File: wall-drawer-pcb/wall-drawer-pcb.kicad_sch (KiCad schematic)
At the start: 13 parts, among them J1 Conn_01x04_Pin, J2 Conn_01x04_Pin, J3 Conn_01x02_Pin, J4 Conn_01x02_Pin, J5 Conn_PWRJack_2x5.5mm_CUIDevic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, M1 Module_XIAO-ESP32C3, U1 Regulator_Linear_5.0V_1A_OnSe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

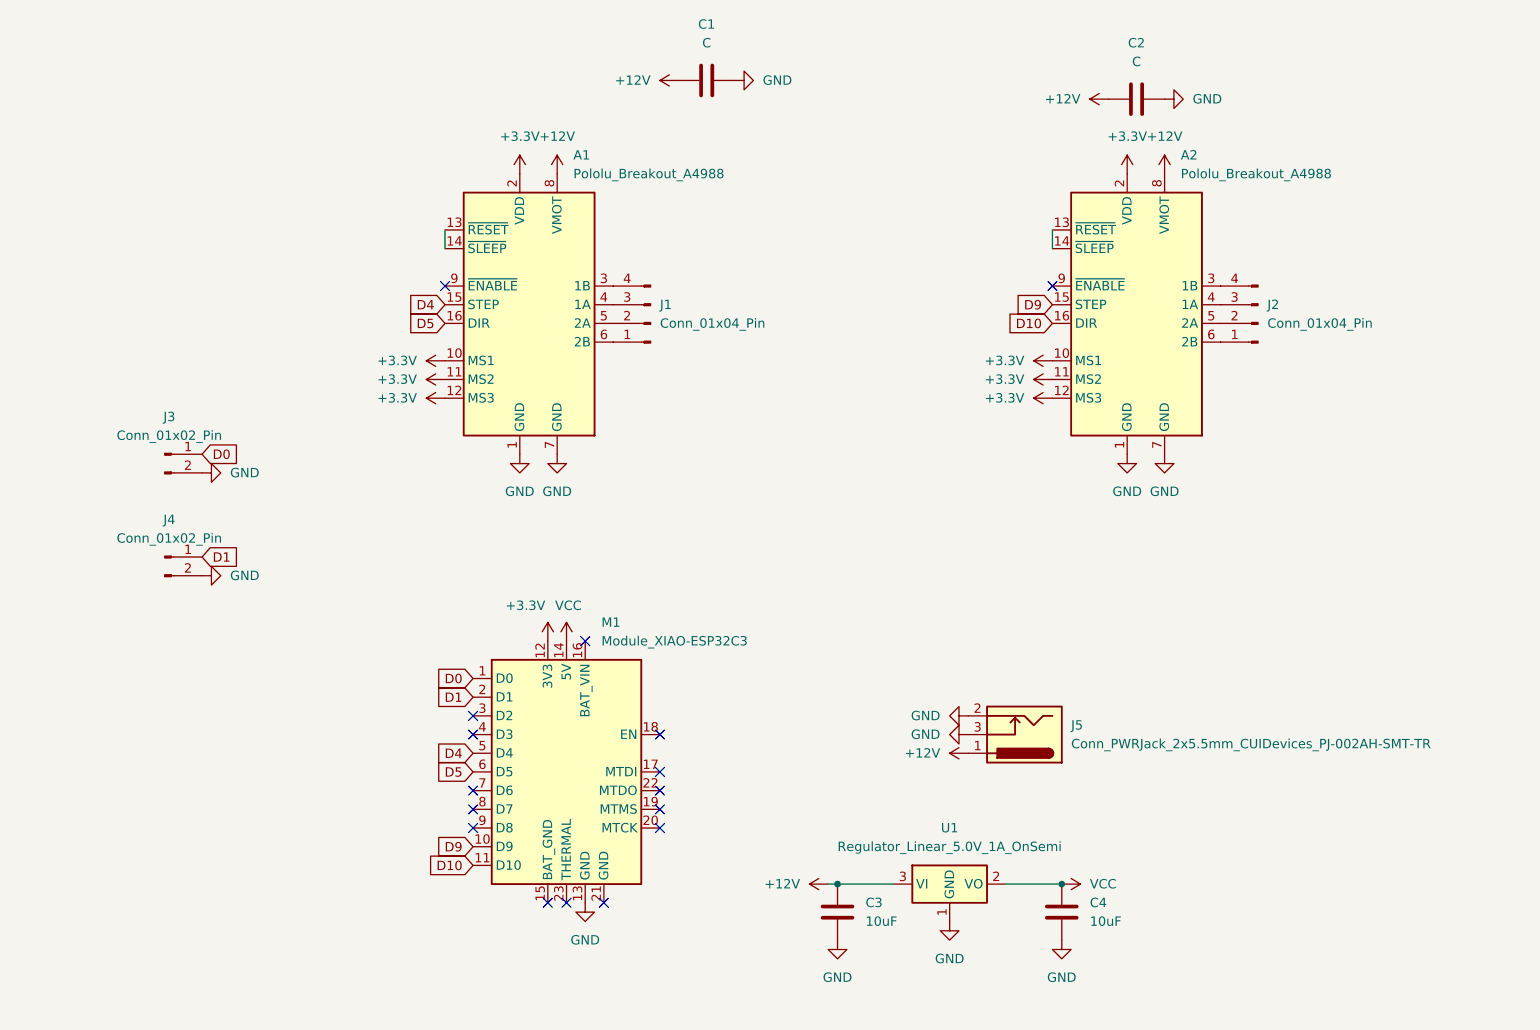
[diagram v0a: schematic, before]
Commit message: wall drawer pcb to use tmc2209s
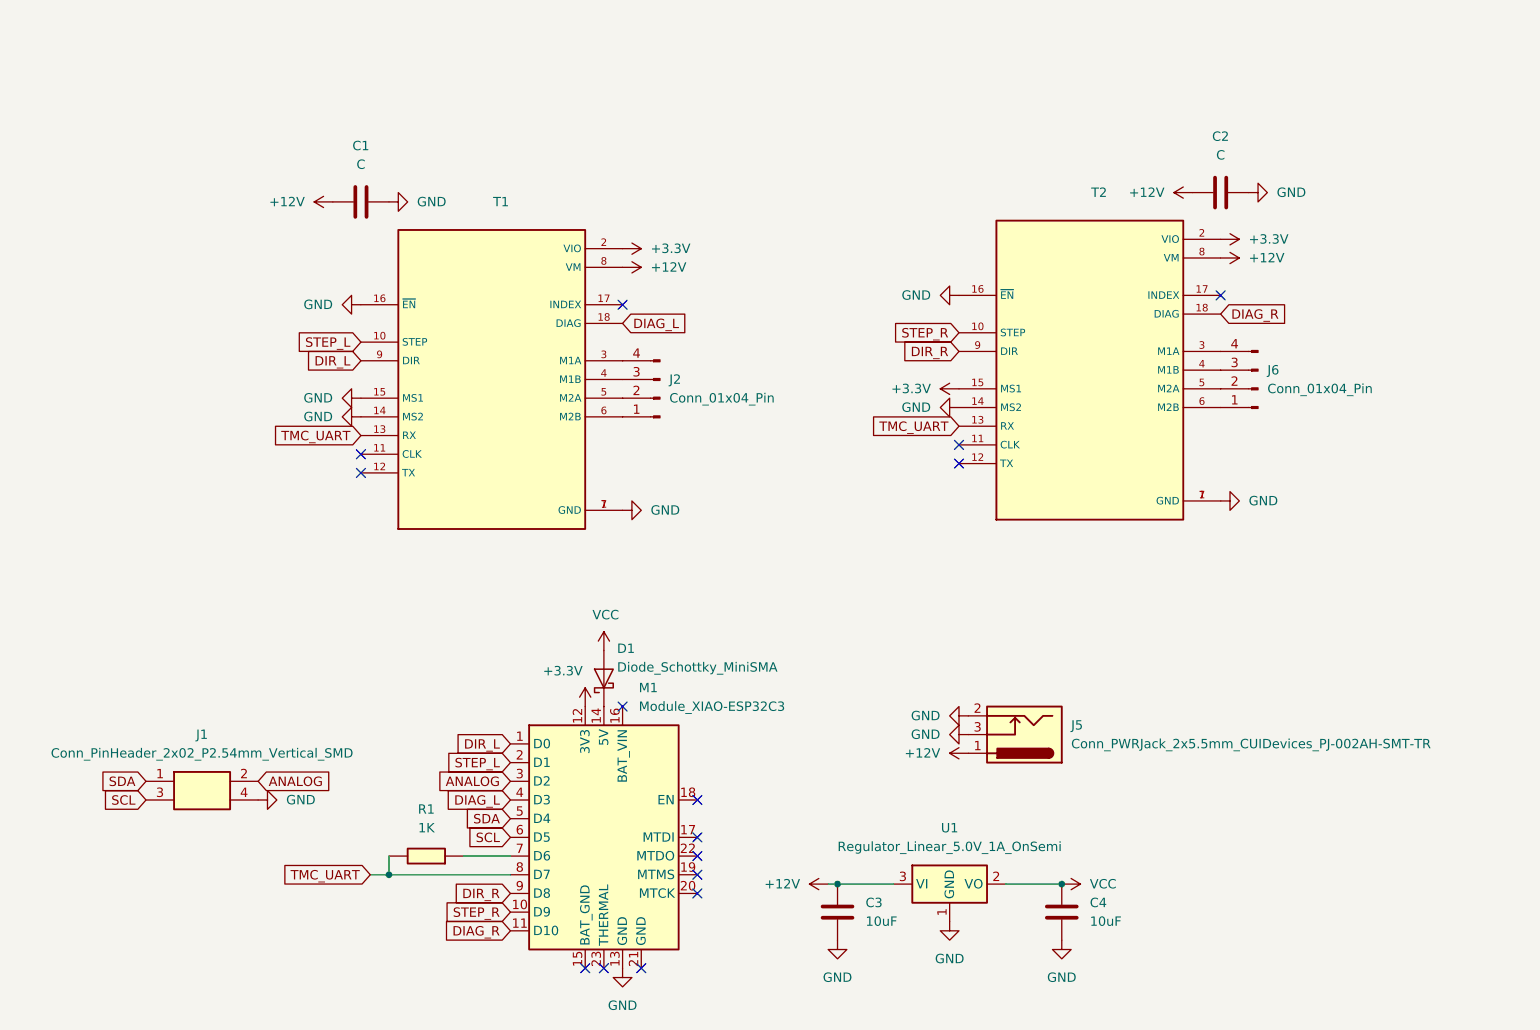
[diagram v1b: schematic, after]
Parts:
- removed A1, A2: Pololu_Breakout_A4988, Module:Pololu_Breakout-16_15.2x20.3mm, symbol Driver_Motor:Pololu_Breakout_A4988
- removed J1: Conn_01x04_Pin, Connector_PinHeader_2.54mm:PinHeader_1x04_P2.54mm_Vertical, symbol Connector:Conn_01x04_Pin
- removed J3, J4: Conn_01x02_Pin, Connector_PinHeader_2.54mm:PinHeader_1x02_P2.54mm_Vertical, symbol Connector:Conn_01x02_Pin
- added D1: Diode_Schottky_MiniSMA, fab:Diode_Schottky_MiniSMA, symbol fab:Diode_Schottky_MiniSMA
- added J1: Conn_PinHeader_2x02_P2.54mm_Vertical_SMD, fab:PinHeader_2x02_P2.54mm_Vertical_SMD, symbol fab:Conn_PinHeader_2x02_P2.54mm_Vertical_SMD
- added J6: Conn_01x04_Pin, Connector_PinHeader_2.54mm:PinHeader_1x04_P2.54mm_Vertical, symbol Connector:Conn_01x04_Pin
- added R1: 1K, fab:R_1206, symbol fab:R_1206
- added T1, T2: ~, TMC2209_SILENTSTEPSTICK:MODULE_TMC2209_SILENTSTEPSTICK, symbol TMC2209_SILENTSTEPSTICK:BTT_TMC2209
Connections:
- net +12V: now also T1.8 (VM), T2.8 (VM)
- net +3.3V: now also T1.2 (VIO), T2.15 (MS1), T2.2 (VIO)
- net GND: now also J1.4 (Pin_4), T1.1 (GND), T1.14 (MS2), T1.15 (MS1), T1.16 (~{EN}), T1.7 (GND), T2.1 (GND), T2.14 (MS2), T2.16 (~{EN}), T2.7 (GND)
- net VCC: now also D1.2 (A); no longer M1.14 (5V)
- net at J2.4 (Pin_4): now also T1.3 (M1A)
- net at J2.3 (Pin_3): now also T1.4 (M1B)
- net at J2.2 (Pin_2): now also T1.5 (M2A)
- net at J2.1 (Pin_1): now also T1.6 (M2B)
- net ANALOG: now reaches M1.3 (D2)
- net ANALOG: now also J1.2 (Pin_2)
- net DIAG_L: now reaches M1.4 (D3)
- net DIAG_L: now also T1.18 (DIAG)
- net at M1.7 (D6): now also R1.2
- net TMC_UART: now reaches M1.8 (D7)
- net TMC_UART: now also R1.1, T1.13 (RX), T2.13 (RX)
- net DIR_R: now reaches M1.9 (D8)
- net DIR_R: now also T2.9 (DIR)
- net D0 renamed DIR_L
- net DIR_L: now also T1.9 (DIR)
- net D1 renamed STEP_L
- net STEP_L: now also T1.10 (STEP)
- net D10 renamed DIAG_R
- net DIAG_R: now also T2.18 (DIAG)
- net D4 renamed SDA
- net SDA: now also J1.1 (Pin_1)
- net D5 renamed SCL
- net SCL: now also J1.3 (Pin_3)
- net D9 renamed STEP_R
- net STEP_R: now also T2.10 (STEP)
- new net: D1.1 (K), M1.14 (5V)
- new net: J6.1 (Pin_1), T2.6 (M2B)
- new net: J6.2 (Pin_2), T2.5 (M2A)
- new net: J6.3 (Pin_3), T2.4 (M1B)
- new net: J6.4 (Pin_4), T2.3 (M1A)
- no-connect marks 16 -> 15
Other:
- moved on the sheet: C1, C2, M1
